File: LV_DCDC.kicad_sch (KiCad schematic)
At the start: 10 parts, among them J1 1017503, J2 1017503

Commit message: did some stuff yesterday i dont remember
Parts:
- removed PS1: DCM3623T36G26C2T00, DCM3623T36G26C2T00:CONV_DCM3623T36G26C2T00, symbol DCM3623T36G26C2T00:DCM3623T36G26C2T00
- added C11, C27, C28, C29, C30, C31: 10uF, symbol Device:C
- added C32: C_Polarized, symbol Device:C_Polarized
- added C33, C34, C35, C36: 1000uF, symbol Device:C_Polarized
- added L4, L5: 1uH, symbol Device:L
- added L6, L7: L, symbol Device:L
- added PS3: DCM3623T36G26C2T00, DCM3623T36G26C2T00:CONV_DCM3623T36G26C2T00, symbol DCM3623T36G26C2T00:DCM3623T36G26C2T00
- added R18, R19: 300mOhm, symbol Device:R
- added R20, R21: 301Ohm, symbol Device:R
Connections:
- net +VDC: now also C32.1, L4.1, L5.1, R18.1, R19.1; no longer PS2.A1 (+IN)
- net GND: now also C33.2, C34.2, C35.2, C36.2, PS3.B2 (-OUT), PS3.D2 (-OUT__1)
- net GNDPWR: now also C11.2, C27.2, C28.2, C29.2, C30.2, C31.2, C32.2, PS3.E1 (-IN)
- net at PS2.A2 (+OUT), PS2.C2 (+OUT__1): now also C33.1, C36.1, L7.1; no longer R17.1
- net at PS2.B1 (TR): now also R20.2
- net at R15.1: now also L6.2
- new net: C11.1, C27.1, C28.1, L4.2, PS3.A1 (+IN), R18.2
- new net: C29.1, C30.1, C31.1, L5.2, PS2.A1 (+IN), R19.2
- new net: C34.1, C35.1, L6.1, PS3.A2 (+OUT), PS3.C2 (+OUT__1)
- new net: PS3.B1 (TR), R21.2
- new net: L7.2, R17.1
- new net Trim: R20.1, R21.1
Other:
- removed sheet CAN
- added sheet trim (trim.kicad_sch)
- sheet power ports: added +3.3V, +5V, Vin; removed none
- sheet uC ports: added none; removed CANRx, CANTx
- note added: "BCM has max external output capacitance of 470uF when load under 20% Each DCM has internal input capacitance of ~30uF + 30uF of ceramics =120uF"
- note added: "figure out how to disable the trim also"
- note added: "maybe add option for both uC- and analog trim"
- moved on the sheet: J1

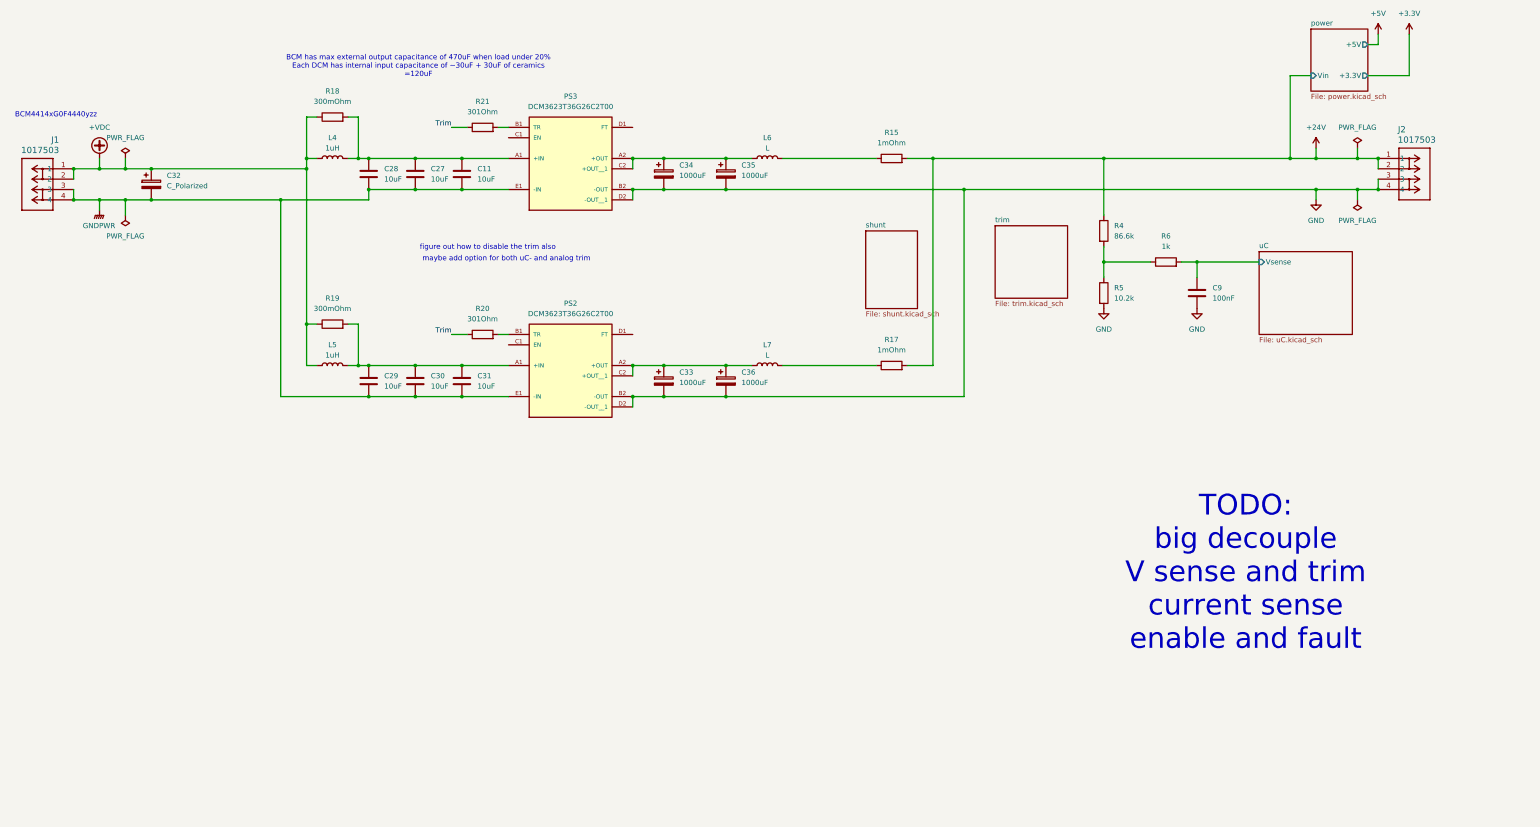
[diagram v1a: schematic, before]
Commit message: Made trim circuit
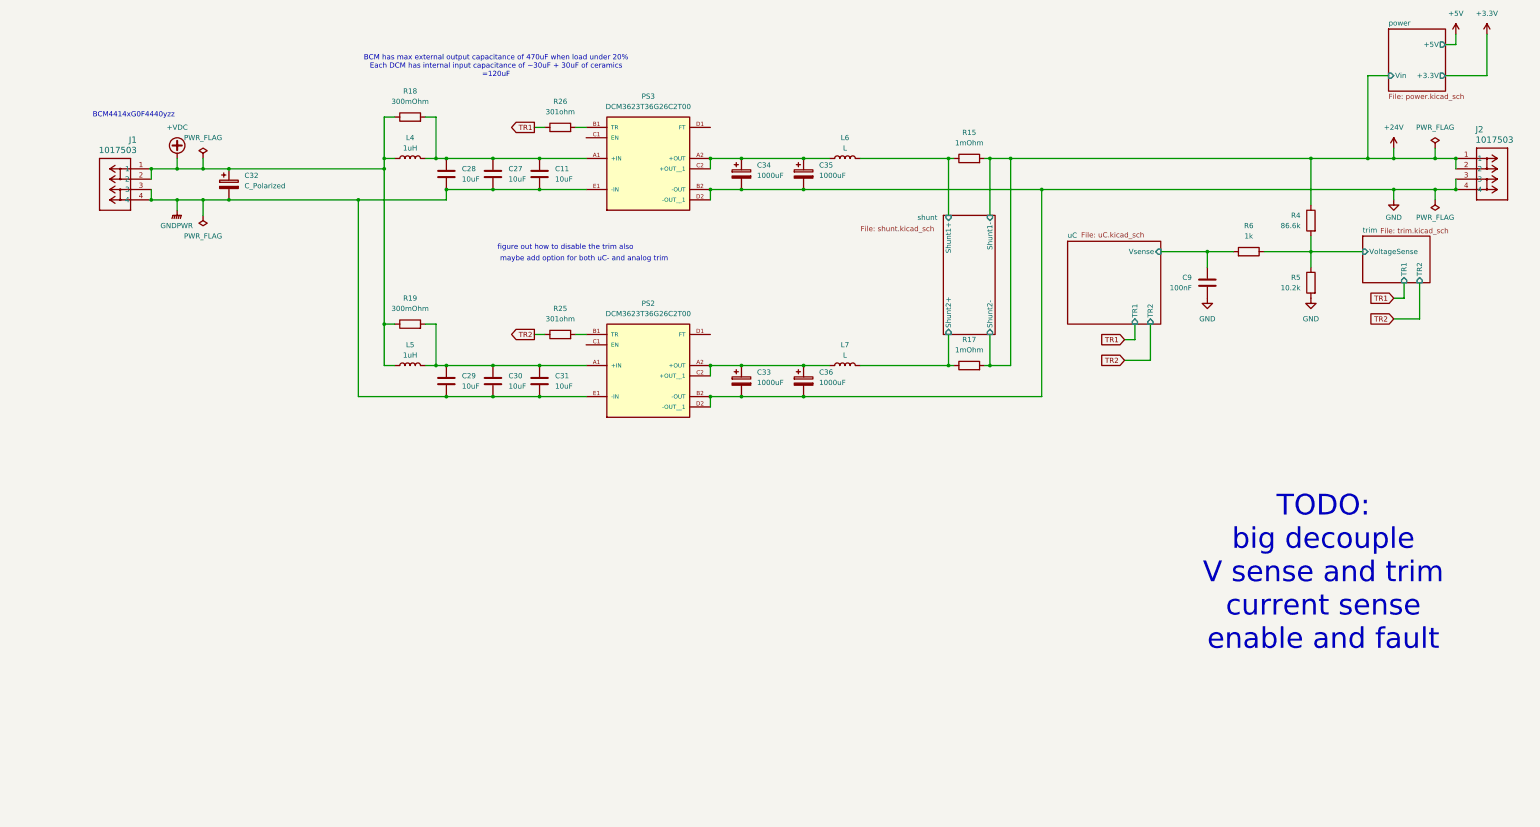
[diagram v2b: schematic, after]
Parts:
- removed R20, R21: 301Ohm, symbol Device:R
- added R25, R26: 301ohm, symbol Device:R
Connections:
- net at PS2.B1 (TR): now also R25.2
- net at PS3.B1 (TR): now also R26.2
- net trim/VoltageSense: now reaches R4.2, R5.1, R6.1
- net shunt/Shunt1+: now reaches L6.2, R15.1
- net shunt/Shunt2+: now reaches L7.2, R17.1
- new net TR1: R26.1
- new net TR2: R25.1
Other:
- sheet shunt ports: added Shunt1+, Shunt1-, Shunt2+, Shunt2-; removed none
- sheet trim ports: added TR1, TR2, VoltageSense; removed none
- sheet uC ports: added TR1, TR2; removed none
- moved on the sheet: C11, C27, C28, C29, C30, C31, C32, C33, C34, C35, C36, C9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

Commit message: added shunts
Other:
- sheet shunt ports: added CurrSense1, CurrSense2; removed none
- note added: "TODO: big decouple enable and fault"
- note removed: "TODO: big decouple V sense and trim current sense enable and fault"
- moved on the sheet: C11, C27, C28, C29, C30, C31, C32, C33, C34, C35, C36, C9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

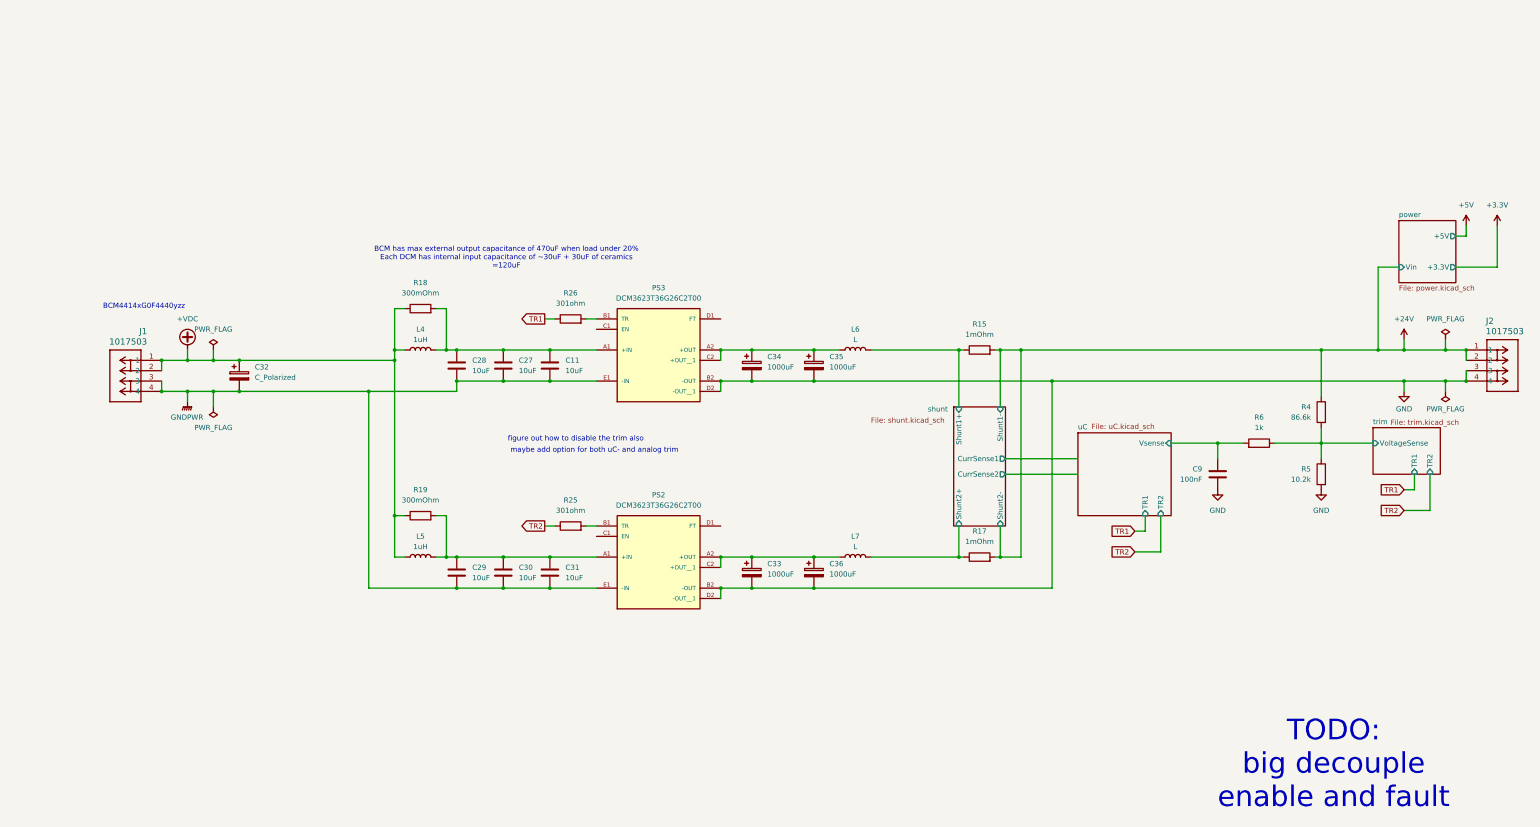
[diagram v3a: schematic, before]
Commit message: assigned footprints, some minor schematic stuff, started layout
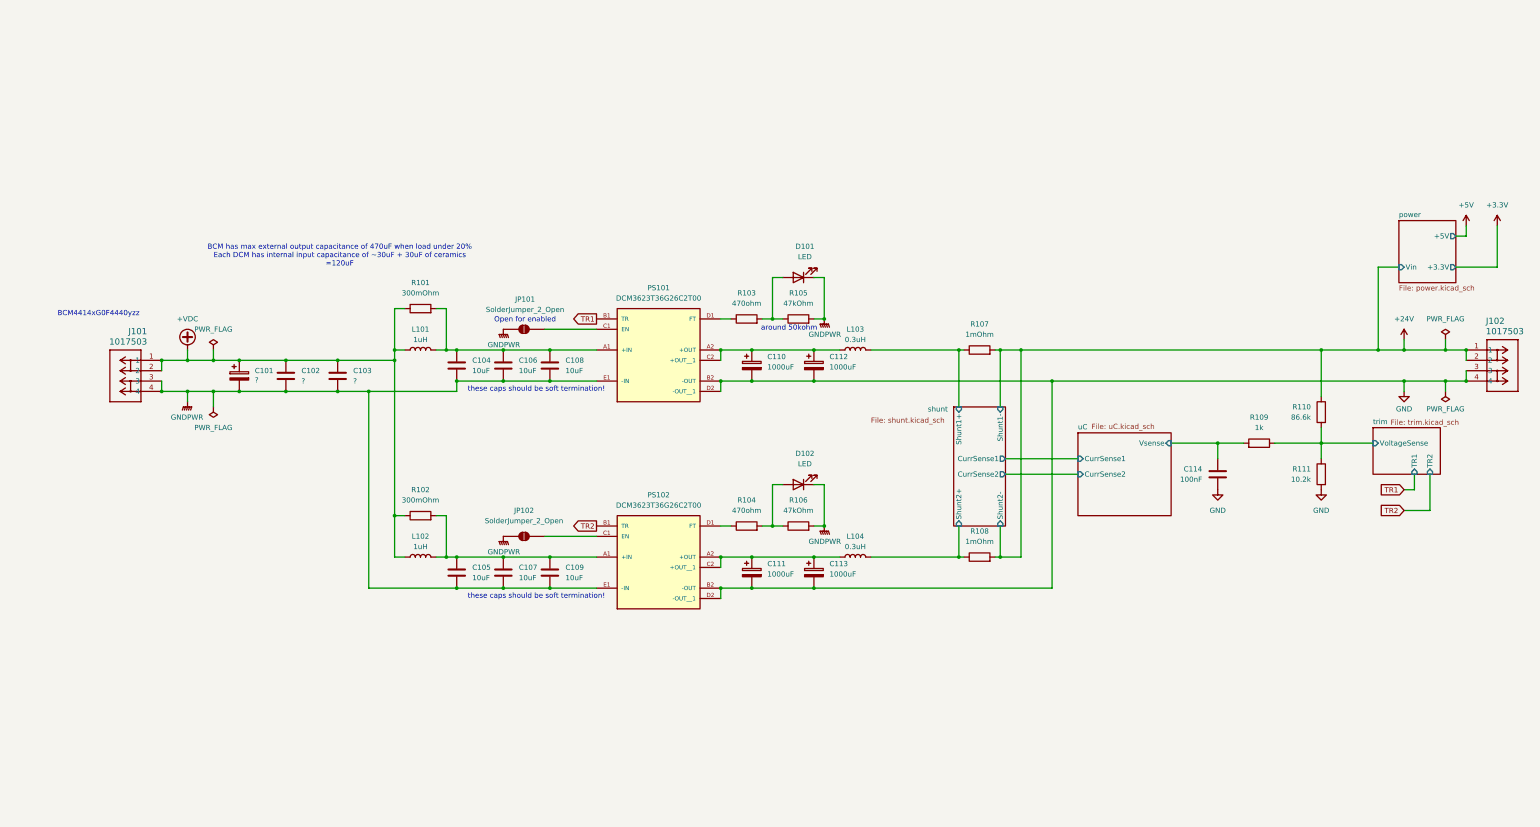
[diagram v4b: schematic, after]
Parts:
- removed R25, R26: 301ohm, symbol Device:R
- added C102, C103: ?, Capacitor_SMD:C_1206_3216Metric, symbol Device:C
- added D101, D102: LED, LED_SMD:LED_0603_1608Metric, symbol Device:LED
- added JP101, JP102: SolderJumper_2_Open, Jumper:SolderJumper-2_P1.3mm_Open_TrianglePad1.0x1.5mm, symbol Jumper:SolderJumper_2_Open
- added R103, R104: 470ohm, Resistor_SMD:R_0603_1608Metric, symbol Device:R
- added R105, R106: 47kOhm, Resistor_SMD:R_0603_1608Metric, symbol Device:R
- C101: renamed from C32; value C_Polarized -> ?; footprint (none) -> Capacitor_THT:CP_Radial_D12.5mm_P5.00mm
- C104: renamed from C28; footprint (none) -> Capacitor_SMD:C_1206_3216Metric
- C105: renamed from C29; footprint (none) -> Capacitor_SMD:C_1206_3216Metric
- C106: renamed from C27; footprint (none) -> Capacitor_SMD:C_1206_3216Metric
- C107: renamed from C30; footprint (none) -> Capacitor_SMD:C_1206_3216Metric
- C108: renamed from C11; footprint (none) -> Capacitor_SMD:C_1206_3216Metric
- C109: renamed from C31; footprint (none) -> Capacitor_SMD:C_1206_3216Metric
- C110: renamed from C34; footprint (none) -> Capacitor_THT:CP_Radial_D12.5mm_P5.00mm
- C111: renamed from C33; footprint (none) -> Capacitor_THT:CP_Radial_D12.5mm_P5.00mm
- C112: renamed from C35; footprint (none) -> Capacitor_THT:CP_Radial_D12.5mm_P5.00mm
- C113: renamed from C36; footprint (none) -> Capacitor_THT:CP_Radial_D12.5mm_P5.00mm
- C114: renamed from C9; footprint (none) -> Capacitor_SMD:C_0603_1608Metric
- J101: renamed from J1; footprint CONN_1017491 -> footprints:CONN_1017491
- J102: renamed from J2; footprint CONN_1017491 -> footprints:CONN_1017491
- L101: renamed from L4; footprint (none) -> Inductor_SMD:L_Bourns_SRP1770TA_16.9x16.9mm
- L102: renamed from L5; footprint (none) -> Inductor_SMD:L_Bourns_SRP1770TA_16.9x16.9mm
- L103: renamed from L6; value L -> 0.3uH; footprint (none) -> Inductor_SMD:L_APV_APH1040
- L104: renamed from L7; value L -> 0.3uH; footprint (none) -> Inductor_SMD:L_APV_APH1040
- PS101: renamed from PS3; footprint DCM3623T36G26C2T00:CONV_DCM3623T36G26C2T00 -> footprints:CONV_DCM3623T36G26C2T00
- PS102: renamed from PS2; footprint DCM3623T36G26C2T00:CONV_DCM3623T36G26C2T00 -> footprints:CONV_DCM3623T36G26C2T00
- R101: renamed from R18; footprint (none) -> Resistor_SMD:R_1206_3216Metric
- R102: renamed from R19; footprint (none) -> Resistor_SMD:R_1206_3216Metric
- R107: renamed from R15; footprint (none) -> Resistor_SMD:R_2512_6332Metric
- R108: renamed from R17; footprint (none) -> Resistor_SMD:R_2512_6332Metric
- R109: renamed from R6; footprint (none) -> Resistor_SMD:R_0603_1608Metric
- R110: renamed from R4; footprint (none) -> Resistor_SMD:R_0603_1608Metric
- R111: renamed from R5; footprint (none) -> Resistor_SMD:R_0603_1608Metric
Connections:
- net +VDC: now also C102.1, C103.1
- net GNDPWR: now also C102.2, C103.2, D101.1 (K), D102.1 (K), JP101.2 (B), JP102.2 (B), R105.2, R106.2
- net TR1: now also PS101.B1 (TR)
- net TR2: now also PS102.B1 (TR)
- net at PS102.C1 (EN): now also JP102.1 (A)
- net at PS102.D1 (FT): now also R104.1
- net at PS101.C1 (EN): now also JP101.1 (A)
- net at PS101.D1 (FT): now also R103.1
- new net: D101.2 (A), R103.2, R105.1
- new net: D102.2 (A), R104.2, R106.1
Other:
- sheet uC ports: added CurrSense1, CurrSense2; removed TR1, TR2
- note added: "Open for enabled"
- note added: "around 50kohm"
- note added: "these caps should be soft termination!"
- note removed: "TODO: big decouple enable and fault"
- note removed: "figure out how to disable the trim also"
- note removed: "maybe add option for both uC- and analog trim"

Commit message: Layout done except for silkscreen
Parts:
- added C114, C115, C116: ?, Capacitor_SMD:C_1206_3216Metric, symbol Device:C
- added NT101, NT102: NetTie_2, NetTie:NetTie-2_SMD_Pad2.0mm, symbol Device:NetTie_2
- renumbered C114 to C117
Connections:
- net +24V: now also C114.1, C115.1, C116.1
- net GND: now also C114.2, C115.2, C116.2, NT101.2, NT102.2; no longer C117.2, R111.2
- new net GNDA: C117.2, NT102.1, R111.2
- new net GNDD: NT101.1
